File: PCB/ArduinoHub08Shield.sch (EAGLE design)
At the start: 2 parts

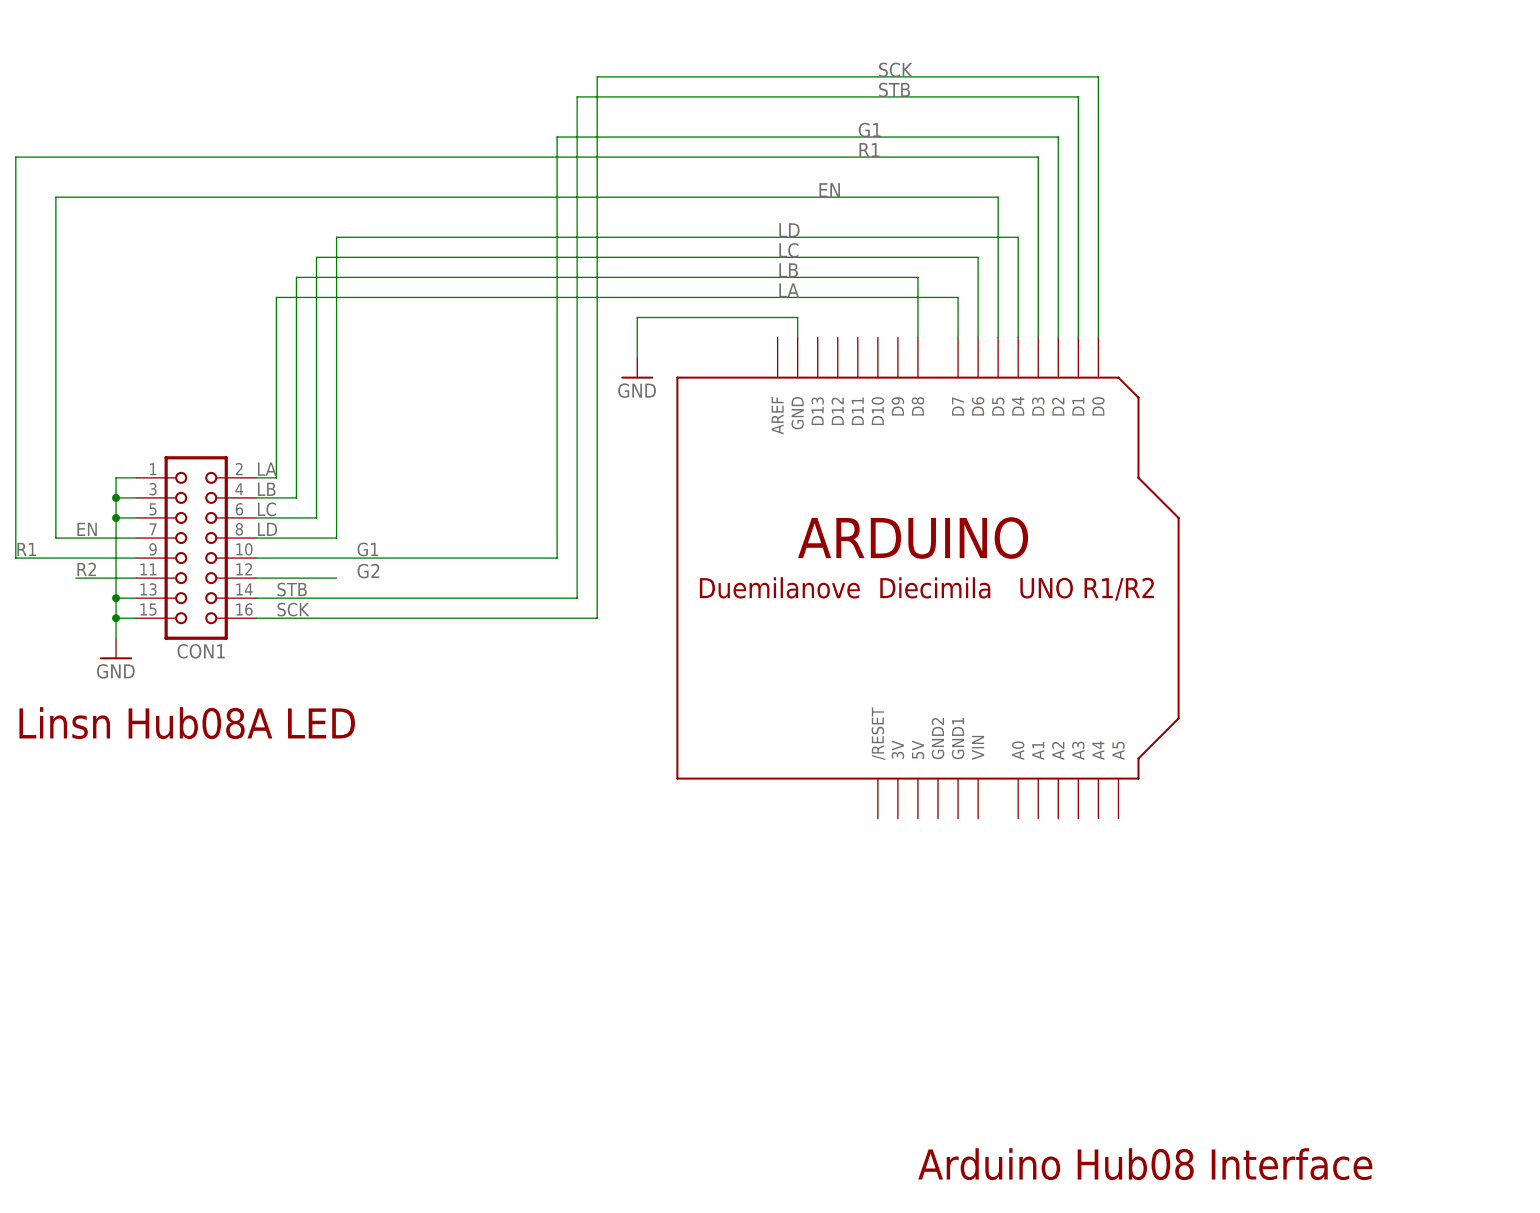
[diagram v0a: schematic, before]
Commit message: Refactoring of the LCDDisplay library
because of the bad performance of the Ultrathin LED_Matrix
library (only about 25 frames/s refresh rate..) the complete
LEDDisplay Library has to be redesigned to talk directly to the
hardware in a more efficient way.
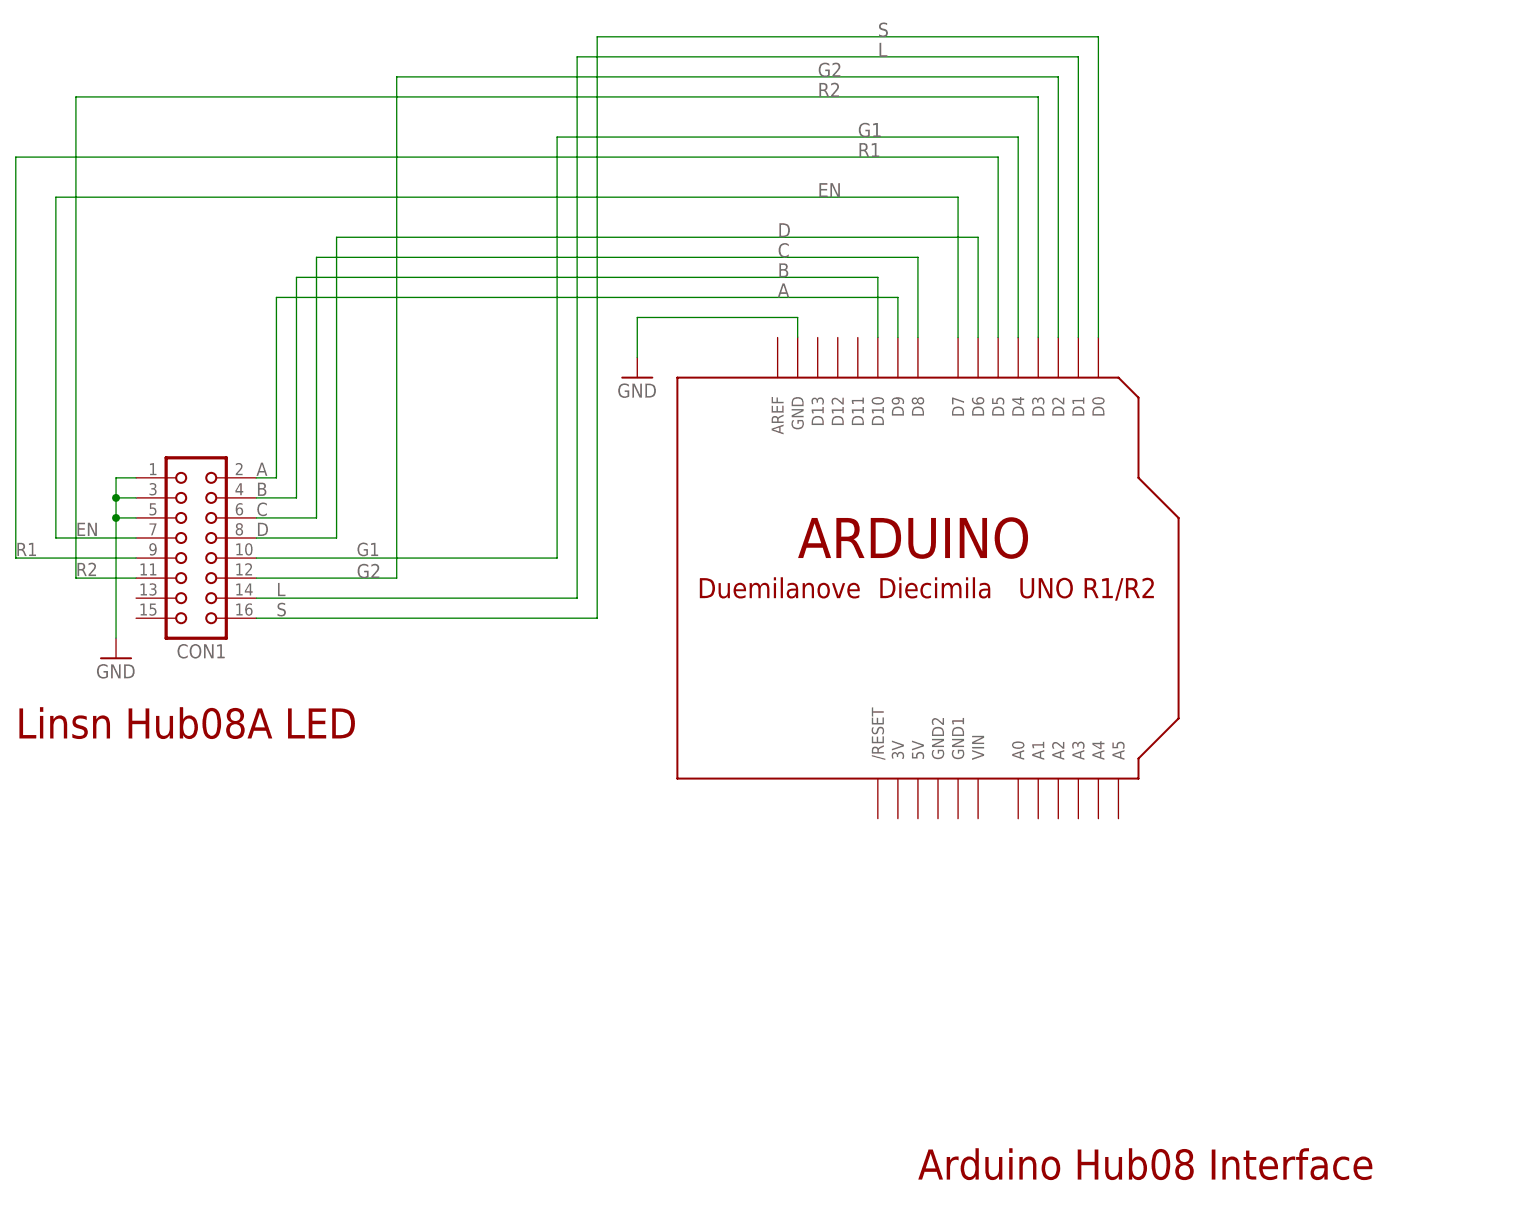
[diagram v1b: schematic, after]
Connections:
- net SCK renamed S
- net STB renamed L
- removed net LA: CON1.2, U$1.D7
- removed net LB: CON1.4, U$1.D8
- removed net LC: CON1.6, U$1.D6
- removed net LD: CON1.8, U$1.D4
- new net A: CON1.2, U$1.D9
- new net B: CON1.4, U$1.D10
- new net C: CON1.6, U$1.D8
- new net D: CON1.8, U$1.D6
- net EN: now also U$1.D7; no longer U$1.D5
- net G1: now also U$1.D4; no longer U$1.D2
- net G2: now also U$1.D2
- net GND: no longer CON1.13, CON1.15
- net R1: now also U$1.D5; no longer U$1.D3
- net R2: now also U$1.D3

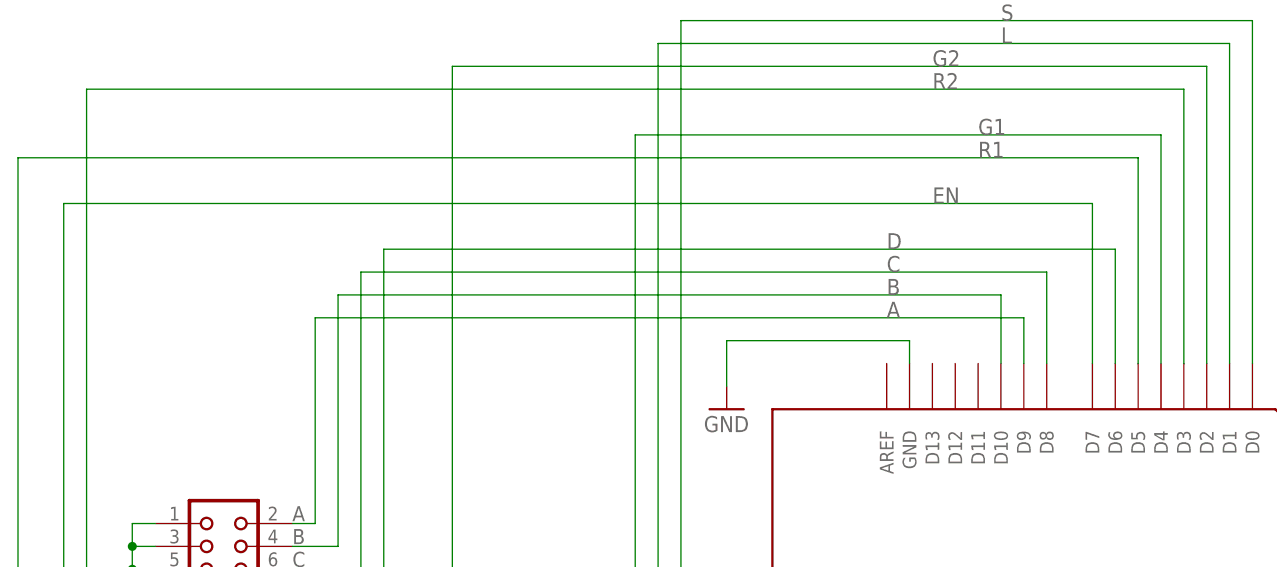
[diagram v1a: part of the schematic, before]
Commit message: isr refactored and fully implemented (tests pending..)
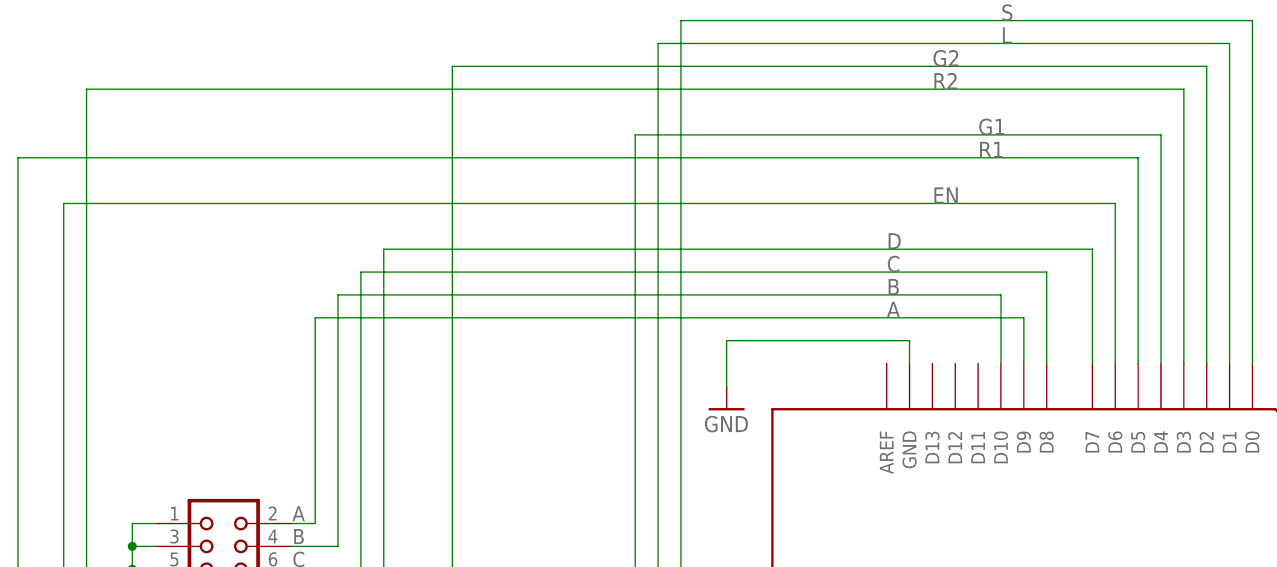
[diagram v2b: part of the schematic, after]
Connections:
- net D: now also U$1.D7; no longer U$1.D6
- net EN: now also U$1.D6; no longer U$1.D7
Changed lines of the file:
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@@
 <label x="91.44" y="109.474" size="1.6764" layer="95"/>
 <wire x1="101.6" y1="109.22" x2="101.6" y2="147.32" width="0.1524" layer="91"/>
-<wire x1="101.6" y1="147.32" x2="182.88" y2="147.32" width="0.1524" layer="91"/>
+<wire x1="101.6" y1="147.32" x2="180.34" y2="147.32" width="0.1524" layer="91"/>
 <label x="157.48" y="147.32" size="1.778" layer="95"/>
-<pinref part="U$1" gate="G$1" pin="D6"/>
-<wire x1="182.88" y1="147.32" x2="182.88" y2="134.62" width="0.1524" layer="91"/>
+<pinref part="U$1" gate="G$1" pin="D7"/>
+<wire x1="180.34" y1="147.32" x2="180.34" y2="134.62" width="0.1524" layer="91"/>
 </segment>
 </net>
@@
 <label x="68.58" y="109.474" size="1.6764" layer="95"/>
 <wire x1="66.04" y1="109.22" x2="66.04" y2="152.4" width="0.1524" layer="91"/>
-<wire x1="66.04" y1="152.4" x2="180.34" y2="152.4" width="0.1524" layer="91"/>
+<wire x1="66.04" y1="152.4" x2="182.88" y2="152.4" width="0.1524" layer="91"/>
 <label x="162.56" y="152.4" size="1.778" layer="95"/>
-<pinref part="U$1" gate="G$1" pin="D7"/>
-<wire x1="180.34" y1="152.4" x2="180.34" y2="134.62" width="0.1524" layer="91"/>
+<pinref part="U$1" gate="G$1" pin="D6"/>
+<wire x1="182.88" y1="152.4" x2="182.88" y2="134.62" width="0.1524" layer="91"/>
 </segment>
 </net>

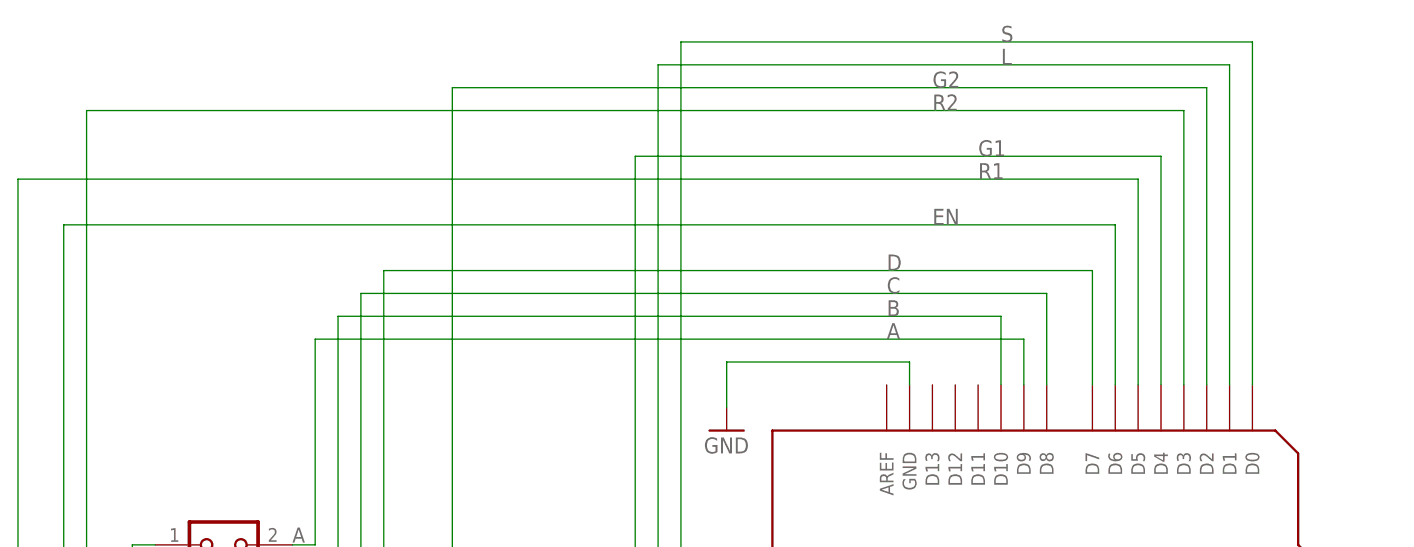
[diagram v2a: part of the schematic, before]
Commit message: another refactoring and code cleanups, see commit msg.
For performance reasons we constraint the usage of the
hardware ports to allow us to be more performant in the
inner loop of the ISR.

The schematic and PCM were changed to adapt these constraints.
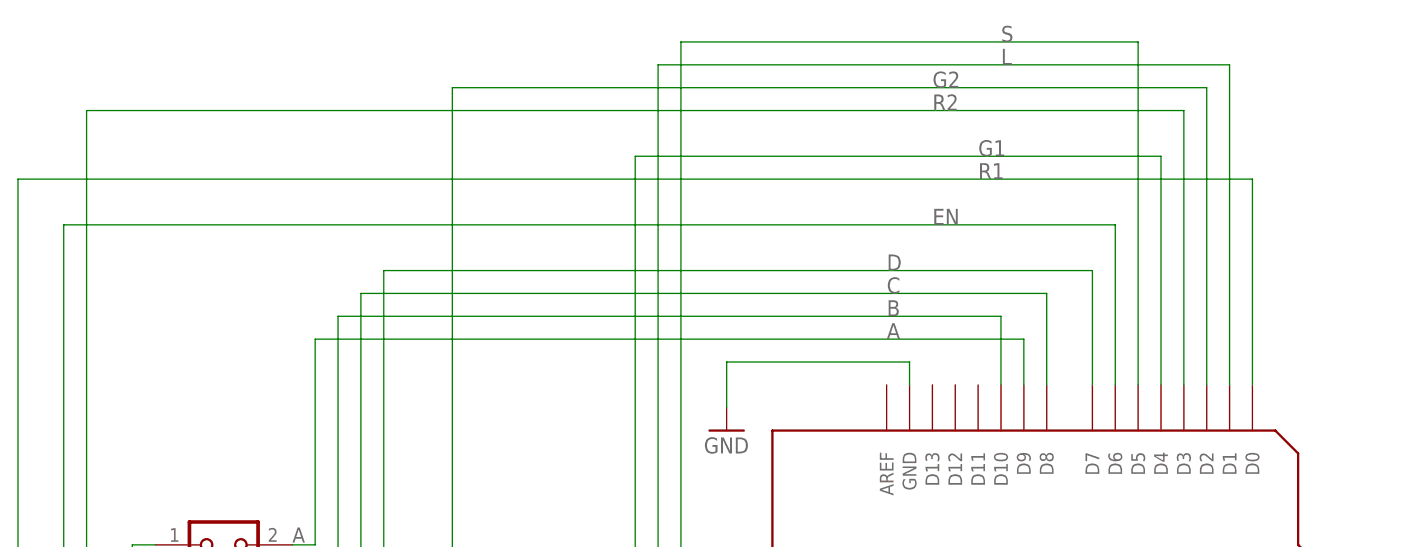
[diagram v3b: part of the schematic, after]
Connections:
- net R1: now also U$1.D0; no longer U$1.D5
- net S: now also U$1.D5; no longer U$1.D0
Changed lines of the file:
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@@
 <label x="60.96" y="106.934" size="1.6764" layer="95"/>
 <wire x1="60.96" y1="106.68" x2="60.96" y2="157.48" width="0.1524" layer="91"/>
-<wire x1="60.96" y1="157.48" x2="185.42" y2="157.48" width="0.1524" layer="91"/>
+<wire x1="60.96" y1="157.48" x2="198.12" y2="157.48" width="0.1524" layer="91"/>
 <label x="167.64" y="157.48" size="1.778" layer="95"/>
-<pinref part="U$1" gate="G$1" pin="D5"/>
-<wire x1="185.42" y1="157.48" x2="185.42" y2="134.62" width="0.1524" layer="91"/>
+<pinref part="U$1" gate="G$1" pin="D0"/>
+<wire x1="198.12" y1="157.48" x2="198.12" y2="134.62" width="0.1524" layer="91"/>
 </segment>
 </net>
@@
 <label x="93.98" y="99.314" size="1.6764" layer="95"/>
 <wire x1="134.62" y1="99.06" x2="134.62" y2="172.72" width="0.1524" layer="91"/>
-<wire x1="134.62" y1="172.72" x2="198.12" y2="172.72" width="0.1524" layer="91"/>
-<pinref part="U$1" gate="G$1" pin="D0"/>
-<wire x1="198.12" y1="172.72" x2="198.12" y2="134.62" width="0.1524" layer="91"/>
+<wire x1="134.62" y1="172.72" x2="185.42" y2="172.72" width="0.1524" layer="91"/>
 <label x="170.18" y="172.72" size="1.778" layer="95"/>
+<pinref part="U$1" gate="G$1" pin="D5"/>
+<wire x1="185.42" y1="172.72" x2="185.42" y2="134.62" width="0.1524" layer="91"/>
 </segment>
 </net>
